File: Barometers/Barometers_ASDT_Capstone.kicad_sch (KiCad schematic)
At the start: 6 parts

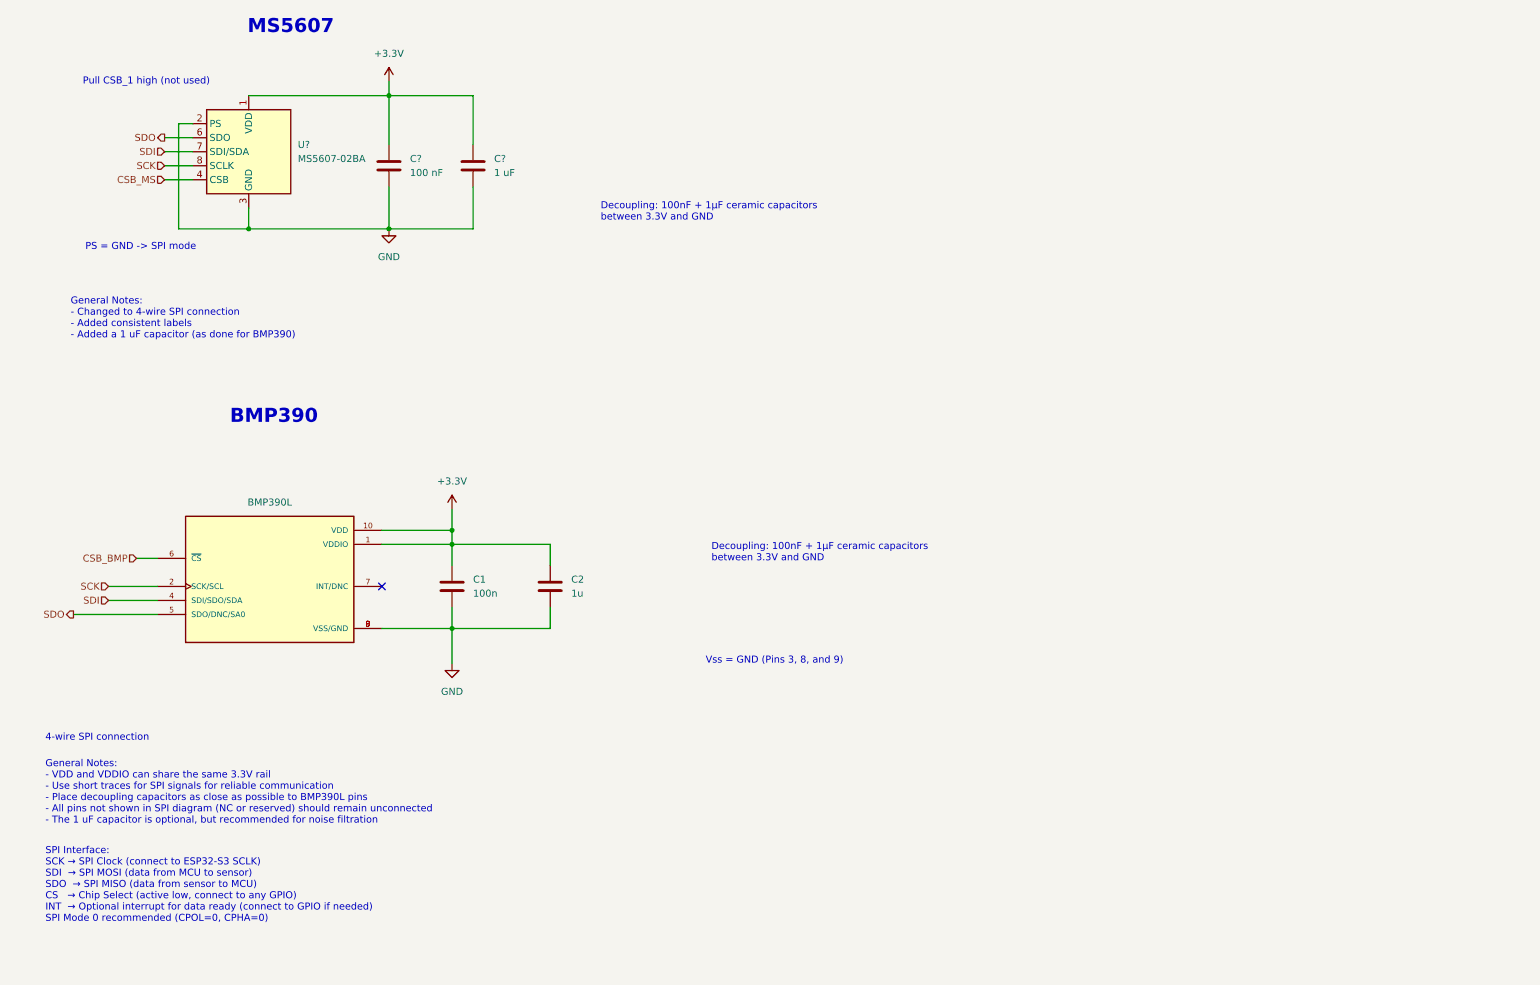
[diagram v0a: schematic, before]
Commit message: Organization and LSM6DSO32 (IMU) schematic
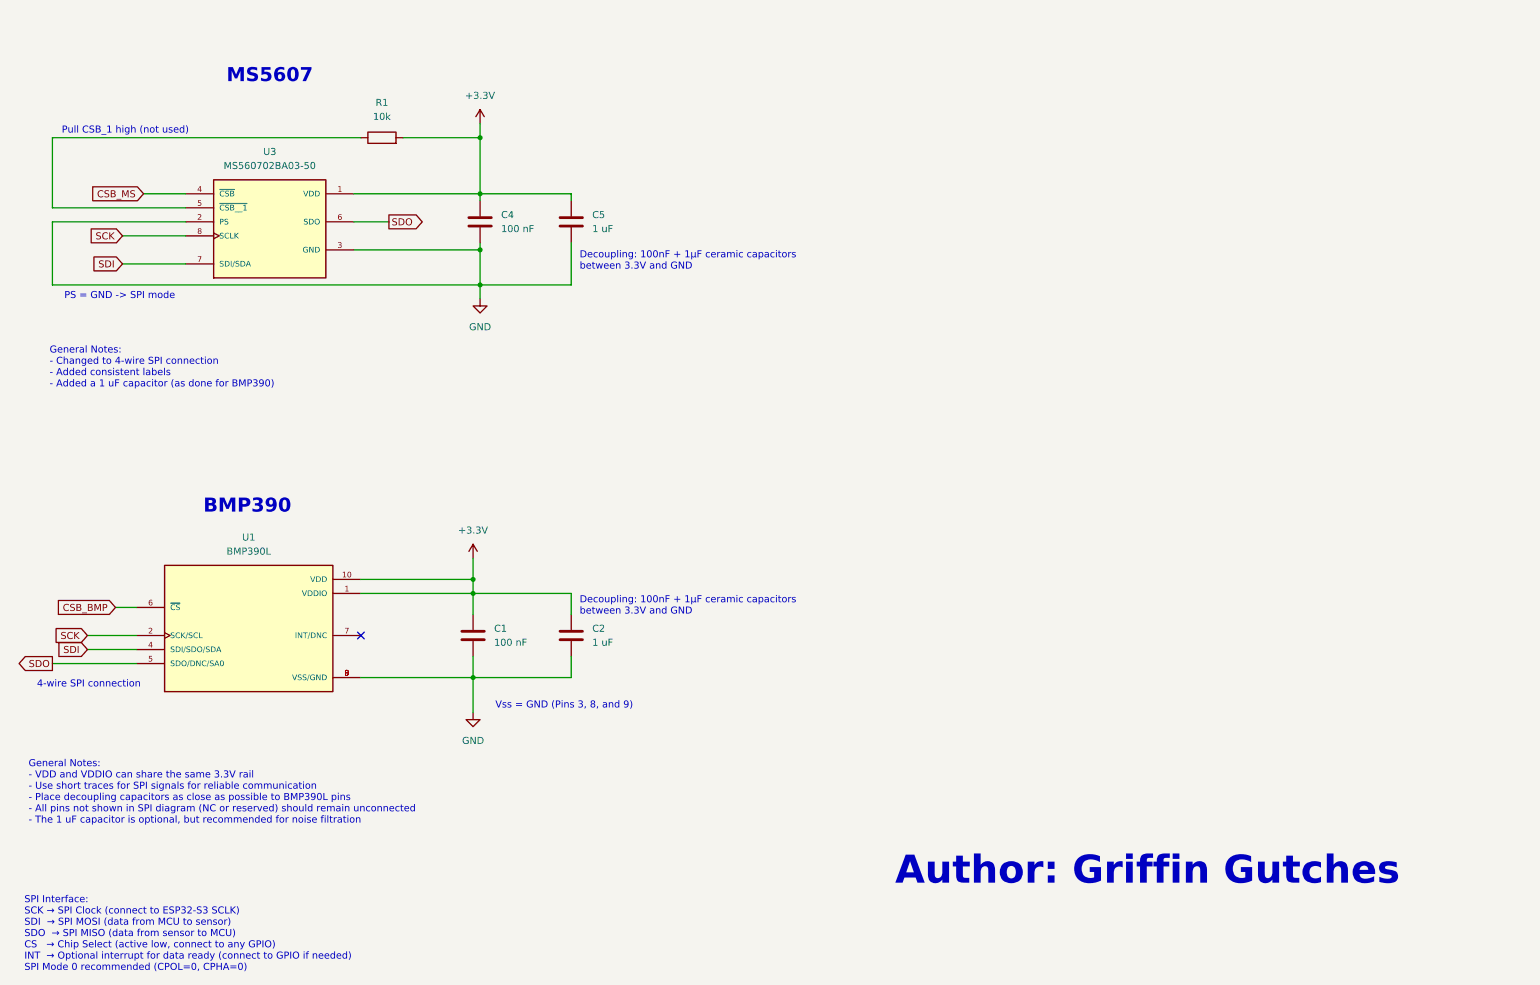
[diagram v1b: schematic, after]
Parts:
- removed C?: 100 nF, Capacitor_SMD:C_0402_1005Metric, symbol Device:C
- removed C?: 1 uF, Capacitor_SMD:C_0402_1005Metric, symbol Device:C
- removed U?: MS5607-02BA, Package_LGA:LGA-8_3x5mm_P1.25mm, symbol Sensor_Pressure:MS5607-02BA
- removed U?: BMP390L, BMP390L:XDCR_BMP390L, symbol BMP390L:BMP390L
- added C4: 100 nF, symbol Device:C
- added C5: 1 uF, symbol Device:C
- added R1: 10k, symbol Device:R
- added U1: BMP390L, BMP390L:XDCR_BMP390L, symbol BMP390L:BMP390L
- added U3: MS560702BA03-50, MS56:SON8_MS5611_TEC, symbol MS560702BA03-50:MS560702BA03-50
- C1: value 100n -> 100 nF; footprint Capacitor_SMD:C_0402_1005Metric -> (none)
- C2: value 1u -> 1 uF; footprint Capacitor_SMD:C_0402_1005Metric -> (none)
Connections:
- net +3.3V: now also C4.1, C5.1, R1.2, U1.1 (VDDIO), U1.10 (VDD), U3.1 (VDD)
- net CSB_BMP: now also U1.6 (~{CS})
- net CSB_MS: now also U3.4 (~{CSB})
- net GND: now also C4.2, C5.2, U1.3 (VSS/GND), U1.8 (VSS/GND), U1.9 (VSS/GND), U3.2 (PS), U3.3 (GND)
- net SCK: now also U1.2 (SCK/SCL), U3.8 (SCLK)
- net SDI: now also U1.4 (SDI/SDO/SDA), U3.7 (SDI/SDA)
- net SDO: now also U1.5 (SDO/DNC/SA0), U3.6 (SDO)
- new net: R1.1, U3.5 (~{CSB__1})
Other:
- note added: "Author: Griffin Gutches"
- company: (none) -> Oregon State University 
- title: (none) -> Barometer Schematics 
